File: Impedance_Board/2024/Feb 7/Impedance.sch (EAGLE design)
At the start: 47 parts, among them U2 INA826AID, U3 MC74VHC1GT66DTT1, U4 MC74VHC1GT66DTT1, U7 AD8606ARZ, U8 AD8606ARZ

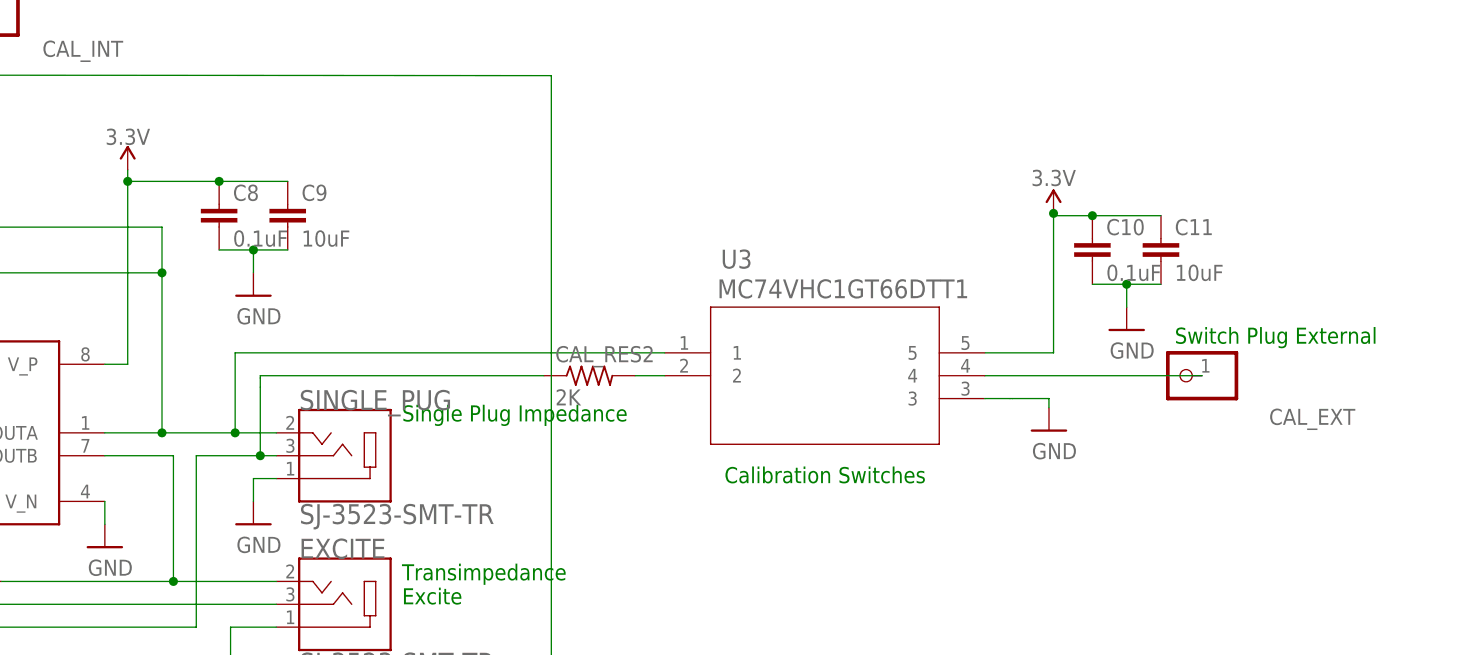
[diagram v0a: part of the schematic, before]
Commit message: Updated SPO2
Crosse Checked with Data Sheet and Evaluation Board
Added 10Ohm resistors in data lines
Adjusted capacitors
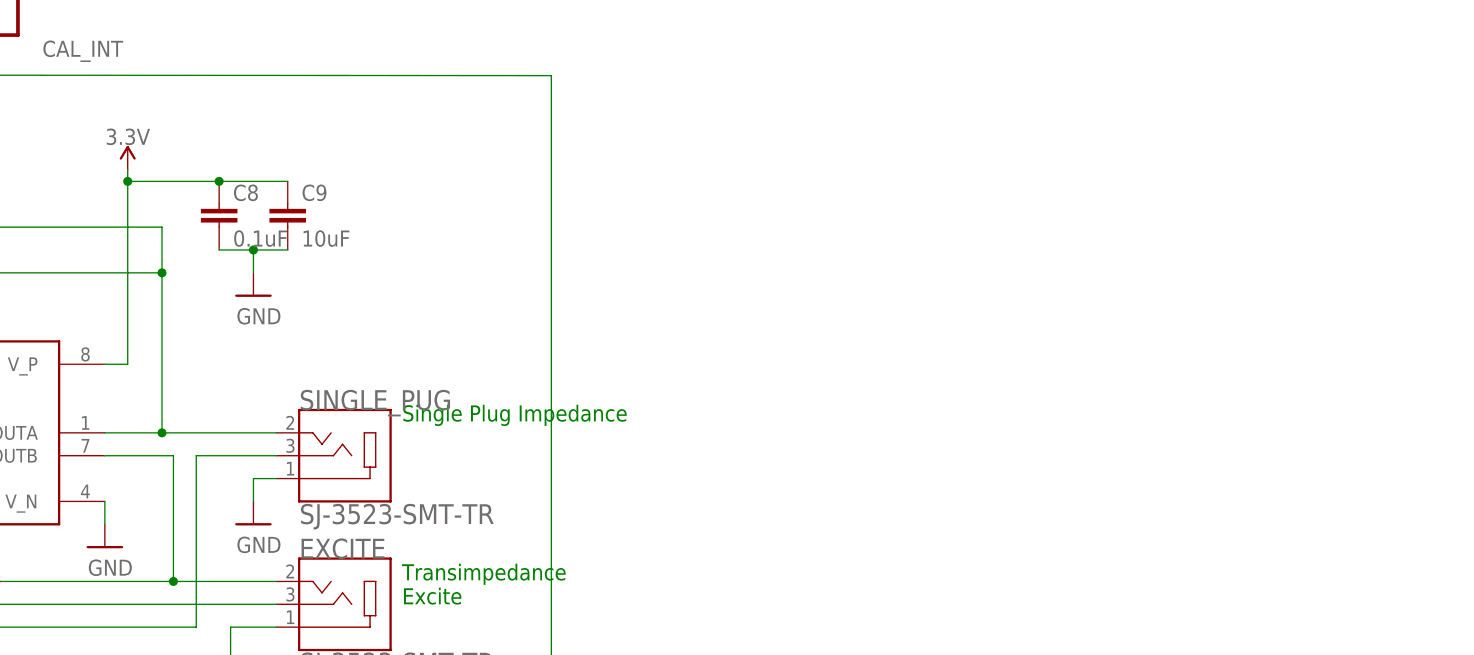
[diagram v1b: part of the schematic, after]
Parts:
- removed C10: 0.1uF, rcl:C-EUC0603
- removed C11: 10uF, rcl:C-EUC0603
- removed CAL_EXT: (no value), pinhead:PINHD-1X1
- removed CAL_RES2: 2K, rcl:R-US_R0603
- removed U3: MC74VHC1GT66DTT1, MC74VHC1GT66DTT1:MC74VHC1GT66DTT1
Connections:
- removed net N$22: CAL_RES2.2, U3.2
- removed net N$27: CAL_EXT.1, U3.4
- net 3.3V: no longer C10.1, C11.1, U3.5
- net GND: no longer C10.2, C11.2, U3.3
- net N$15: no longer U3.1
- net N$17: no longer CAL_RES2.1
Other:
- note removed: "Calibration Switches"
- note removed: "Switch Plug External"
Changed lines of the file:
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@@
 <setting verticaltext="up"/>
 </settings>
-<grid distance="0.1" unitdist="mm" unit="mm" style="lines" multiple="1" display="yes" altdistance="0.2" altunitdist="mm" altunit="mm"/>
+<grid distance="0.1" unitdist="inch" unit="inch" style="lines" multiple="1" display="no" altdistance="0.01" altunitdist="inch" altunit="inch"/>
 <layers>
 <layer number="1" name="Top" color="4" fill="1" visible="no" active="no"/>
@@
 <part name="SUPPLY19" library="SparkFun-PowerSymbols" deviceset="3.3V" device=""/>
 <part name="GND12" library="SparkFun-PowerSymbols" deviceset="GND" device=""/>
-<part name="U3" library="MC74VHC1GT66DTT1" deviceset="MC74VHC1GT66DTT1" device=""/>
 <part name="U4" library="MC74VHC1GT66DTT1" deviceset="MC74VHC1GT66DTT1" device=""/>
-<part name="CAL_RES2" library="rcl" library_urn="urn:adsk.eagle:library:334" deviceset="R-US_" device="R0603" package3d_urn="urn:adsk.eagle:package:23555/3" value="2K"/>
-<part name="SUPPLY20" library="supply1" library_urn="urn:adsk.eagle:library:371" deviceset="GND" device=""/>
-<part name="SUPPLY21" library="SparkFun-PowerSymbols" library_urn="urn:adsk.eagle:library:530" deviceset="3.3V" device=""/>
-<part name="CAL_EXT" library="pinhead" library_urn="urn:adsk.eagle:library:325" deviceset="PINHD-1X1" device="" package3d_urn="urn:adsk.eagle:package:22485/2"/>
 <part name="CAL_RES1" library="rcl" library_urn="urn:adsk.eagle:library:334" deviceset="R-US_" device="R0603" package3d_urn="urn:adsk.eagle:package:23555/3" value="2K"/>
 <part name="SUPPLY22" library="supply1" library_urn="urn:adsk.eagle:library:371" deviceset="GND" device=""/>
@@
 <part name="I2C_OUT" library="adafruit_electromech" deviceset="STEMMA_I2C" device="_QTRA" value="STEMMA_I2C_QTRA"/>
 <part name="TP1" library="SparkFun-Connectors" library_urn="urn:adsk.eagle:library:513" deviceset="TEST-POINT" device="3X5" package3d_urn="urn:adsk.eagle:package:38285/1"/>
-<part name="C10" library="rcl" library_urn="urn:adsk.eagle:library:334" deviceset="C-EU" device="C0603" package3d_urn="urn:adsk.eagle:package:23616/2" value="0.1uF"/>
-<part name="C11" library="rcl" library_urn="urn:adsk.eagle:library:334" deviceset="C-EU" device="C0603" package3d_urn="urn:adsk.eagle:package:23616/2" value="10uF"/>
-<part name="SUPPLY25" library="supply1" library_urn="urn:adsk.eagle:library:371" deviceset="GND" device=""/>
 <part name="C12" library="rcl" library_urn="urn:adsk.eagle:library:334" deviceset="C-EU" device="C0603" package3d_urn="urn:adsk.eagle:package:23616/2" value="0.1uF"/>
 <part name="C13" library="rcl" library_urn="urn:adsk.eagle:library:334" deviceset="C-EU" device="C0603" package3d_urn="urn:adsk.eagle:package:23616/2" value="10uF"/>
@@
 <text x="-38.1" y="-74.93" size="1.778" layer="91">Amplifier</text>
 <text x="-30.48" y="-46.99" size="1.778" layer="91">Buffer</text>
-<text x="191.262" y="13.716" size="1.778" layer="91">Switch Plug External</text>
-<text x="141.224" y="-1.778" size="1.778" layer="91">Calibration Switches</text>
 <text x="-113.538" y="15.748" size="1.778" layer="91">STEMMA QT Connectors</text>
 <text x="-106.68" y="-29.464" size="1.778" layer="91">I2C Through-Holes</text>
@@
 <attribute name="VALUE" x="-77.47" y="-5.334" size="1.778" layer="96" font="vector" align="top-center"/>
 </instance>
-<instance part="U3" gate="A" x="132.08" y="12.7" smashed="yes">
-<attribute name="NAME" x="140.8176" y="22.0726" size="2.0828" layer="95" ratio="6" rot="SR0"/>
-<attribute name="VALUE" x="140.4366" y="18.7706" size="2.0828" layer="96" ratio="6" rot="SR0"/>
-</instance>
 <instance part="U4" gate="A" x="-2.54" y="68.58" smashed="yes">
 <attribute name="NAME" x="6.1976" y="77.4446" size="2.0828" layer="95" ratio="6" rot="SR0"/>
 <attribute name="VALUE" x="6.3246" y="74.9046" size="2.0828" layer="96" ratio="6" rot="SR0"/>
 </instance>
-<instance part="CAL_RES2" gate="G$1" x="126.238" y="10.16" smashed="yes">
-<attribute name="NAME" x="122.428" y="11.6586" size="1.778" layer="95"/>
-<attribute name="VALUE" x="122.428" y="6.858" size="1.778" layer="96"/>
-</instance>
-<instance part="SUPPLY20" gate="1" x="177.292" y="4.064" smashed="yes">
-<attribute name="VALUE" x="175.387" y="0.889" size="1.778" layer="96"/>
-</instance>
-<instance part="SUPPLY21" gate="G$1" x="177.8" y="28.194" smashed="yes">
-<attribute name="VALUE" x="177.8" y="31.242" size="1.778" layer="96" align="bottom-center"/>
-</instance>
-<instance part="CAL_EXT" gate="G$1" x="191.77" y="10.16" smashed="yes" rot="R180">
-<attribute name="NAME" x="211.328" y="6.477" size="1.778" layer="95" rot="R180"/>
-<attribute name="VALUE" x="198.12" y="15.24" size="1.778" layer="96" rot="R180"/>
-</instance>
 <instance part="CAL_RES1" gate="G$1" x="-49.276" y="52.324" smashed="yes" rot="R90">
 <attribute name="NAME" x="-50.7746" y="48.514" size="1.778" layer="95" rot="R90"/>
@@
 <attribute name="NAME" x="-38.354" y="24.892" size="1.778" layer="95" font="vector"/>
 <attribute name="VALUE" x="-38.354" y="19.812" size="1.778" layer="96" font="vector"/>
-</instance>
-<instance part="C10" gate="G$1" x="182.118" y="25.4" smashed="yes">
-<attribute name="NAME" x="183.642" y="25.781" size="1.778" layer="95"/>
-<attribute name="VALUE" x="183.642" y="20.701" size="1.778" layer="96"/>
-</instance>
-<instance part="C11" gate="G$1" x="189.738" y="25.4" smashed="yes">
-<attribute name="NAME" x="191.262" y="25.781" size="1.778" layer="95"/>
-<attribute name="VALUE" x="191.262" y="20.701" size="1.778" layer="96"/>
-</instance>
-<instance part="SUPPLY25" gate="1" x="185.928" y="15.24" smashed="yes">
-<attribute name="VALUE" x="184.023" y="12.065" size="1.778" layer="96"/>
 </instance>
 <instance part="C12" gate="G$1" x="53.34" y="69.85" smashed="yes">
@@
 </segment>
 <segment>
-<pinref part="U3" gate="A" pin="3"/>
-<wire x1="170.18" y1="7.62" x2="172.974" y2="7.62" width="0.1524" layer="91"/>
-<pinref part="SUPPLY20" gate="1" pin="GND"/>
-<wire x1="172.974" y1="7.62" x2="173.228" y2="7.62" width="0.1524" layer="91"/>
-<wire x1="173.228" y1="7.62" x2="177.292" y2="7.62" width="0.1524" layer="91"/>
-<wire x1="177.292" y1="7.62" x2="177.292" y2="6.604" width="0.1524" layer="91"/>
-</segment>
-<segment>
 <pinref part="U4" gate="A" pin="3"/>
 <wire x1="35.56" y1="63.5" x2="42.164" y2="63.5" width="0.1524" layer="91"/>
@@
 <pinref part="SUPPLY22" gate="1" pin="GND"/>
 <wire x1="42.164" y1="60.706" x2="42.164" y2="60.198" width="0.1524" layer="91"/>
-</segment>
-<segment>
-<pinref part="C10" gate="G$1" pin="2"/>
-<pinref part="C11" gate="G$1" pin="2"/>
-<wire x1="182.118" y1="20.32" x2="185.928" y2="20.32" width="0.1524" layer="91"/>
-<wire x1="185.928" y1="20.32" x2="189.738" y2="20.32" width="0.1524" layer="91"/>
-<wire x1="185.928" y1="20.32" x2="185.928" y2="17.78" width="0.1524" layer="91"/>
-<junction x="185.928" y="20.32"/>
-<pinref part="SUPPLY25" gate="1" pin="GND"/>
 </segment>
 <segment>
@@
 <pinref part="I2C_OUT" gate="G$1" pin="V+"/>
 <pinref part="I2C_IN" gate="G$1" pin="V+"/>
-</segment>
-<segment>
-<pinref part="U3" gate="A" pin="5"/>
-<wire x1="170.18" y1="12.7" x2="177.8" y2="12.7" width="0.1524" layer="91"/>
-<wire x1="177.8" y1="12.7" x2="177.8" y2="28.194" width="0.1524" layer="91"/>
-<pinref part="SUPPLY21" gate="G$1" pin="3.3V"/>
-<pinref part="C10" gate="G$1" pin="1"/>
-<wire x1="182.118" y1="27.94" x2="189.738" y2="27.94" width="0.1524" layer="91"/>
-<junction x="182.118" y="27.94"/>
-<pinref part="C11" gate="G$1" pin="1"/>
-<wire x1="182.118" y1="27.94" x2="177.8" y2="27.94" width="0.1524" layer="91"/>
-<wire x1="177.8" y1="27.94" x2="177.8" y2="28.194" width="0.1524" layer="91"/>
-<junction x="177.8" y="28.194"/>
 </segment>
 <segment>
@@
 <wire x1="-45.72" y1="-82.55" x2="-31.78" y2="-82.6" width="0.1524" layer="91"/>
 <pinref part="SINGLE_PUG" gate="G$1" pin="3"/>
-<wire x1="91.44" y1="1.27" x2="89.662" y2="1.27" width="0.1524" layer="91"/>
-<wire x1="89.662" y1="1.27" x2="82.55" y2="1.27" width="0.1524" layer="91"/>
+<wire x1="91.44" y1="1.27" x2="82.55" y2="1.27" width="0.1524" layer="91"/>
 <wire x1="82.55" y1="1.27" x2="82.55" y2="-17.78" width="0.1524" layer="91"/>
 <wire x1="82.55" y1="-17.78" x2="20.32" y2="-17.78" width="0.1524" layer="91"/>
@@
 <wire x1="20.32" y1="-78.74" x2="-45.72" y2="-78.74" width="0.1524" layer="91"/>
 <junction x="-45.72" y="-78.74"/>
-<wire x1="89.662" y1="9.906" x2="89.662" y2="8.89" width="0.1524" layer="91"/>
-<junction x="89.662" y="1.27"/>
-<pinref part="CAL_RES2" gate="G$1" pin="1"/>
-<wire x1="89.662" y1="8.89" x2="89.662" y2="1.27" width="0.1524" layer="91"/>
-<wire x1="89.662" y1="9.906" x2="89.662" y2="10.16" width="0.1524" layer="91"/>
-<wire x1="89.662" y1="10.16" x2="121.158" y2="10.16" width="0.1524" layer="91"/>
 </segment>
 </net>
@@
 <wire x1="59.69" y1="26.67" x2="78.74" y2="26.67" width="0.1524" layer="91"/>
 <pinref part="SINGLE_PUG" gate="G$1" pin="2"/>
-<wire x1="91.44" y1="3.81" x2="86.868" y2="3.81" width="0.1524" layer="91"/>
 <junction x="78.74" y="3.81"/>
-<pinref part="U3" gate="A" pin="1"/>
-<wire x1="86.868" y1="3.81" x2="78.74" y2="3.81" width="0.1524" layer="91"/>
-<wire x1="86.868" y1="3.81" x2="86.868" y2="12.7" width="0.1524" layer="91"/>
-<wire x1="86.868" y1="12.7" x2="134.62" y2="12.7" width="0.1524" layer="91"/>
-<junction x="86.868" y="3.81"/>
+<wire x1="91.44" y1="3.81" x2="78.74" y2="3.81" width="0.1524" layer="91"/>
 </segment>
 </net>
@@
 </segment>
 </net>
-<net name="N$27" class="0">
-<segment>
-<pinref part="U3" gate="A" pin="4"/>
-<pinref part="CAL_EXT" gate="G$1" pin="1"/>
-<wire x1="170.18" y1="10.16" x2="194.31" y2="10.16" width="0.1524" layer="91"/>
-</segment>
-</net>
-<net name="N$22" class="0">
-<segment>
-<pinref part="CAL_RES2" gate="G$1" pin="2"/>
-<pinref part="U3" gate="A" pin="2"/>
-<wire x1="131.318" y1="10.16" x2="134.62" y2="10.16" width="0.1524" layer="91"/>
-</segment>
-</net>
